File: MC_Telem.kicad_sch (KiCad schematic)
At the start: 59 parts, among them J1 Conn_ARM_JTAG_SWD_10, J2 USB_B_Micro, J3 34830-0801, J5 Conn_01x05, J7 DB37_Male_MountingHoles, J8 34830-0801, J9 GPS, Q1 Q_NMOS_GDS, Q2 Q_NMOS_GDS, Q20 AO4407A, U1 STM32F072RBTx, U2 TPS2113, U3 TCAN1042xV, U4 AMS1117-5.0, U5 AMS1117, U6 LSM6DS3, U7 LTC2630, U8 LTC2630, U9 RFD900x

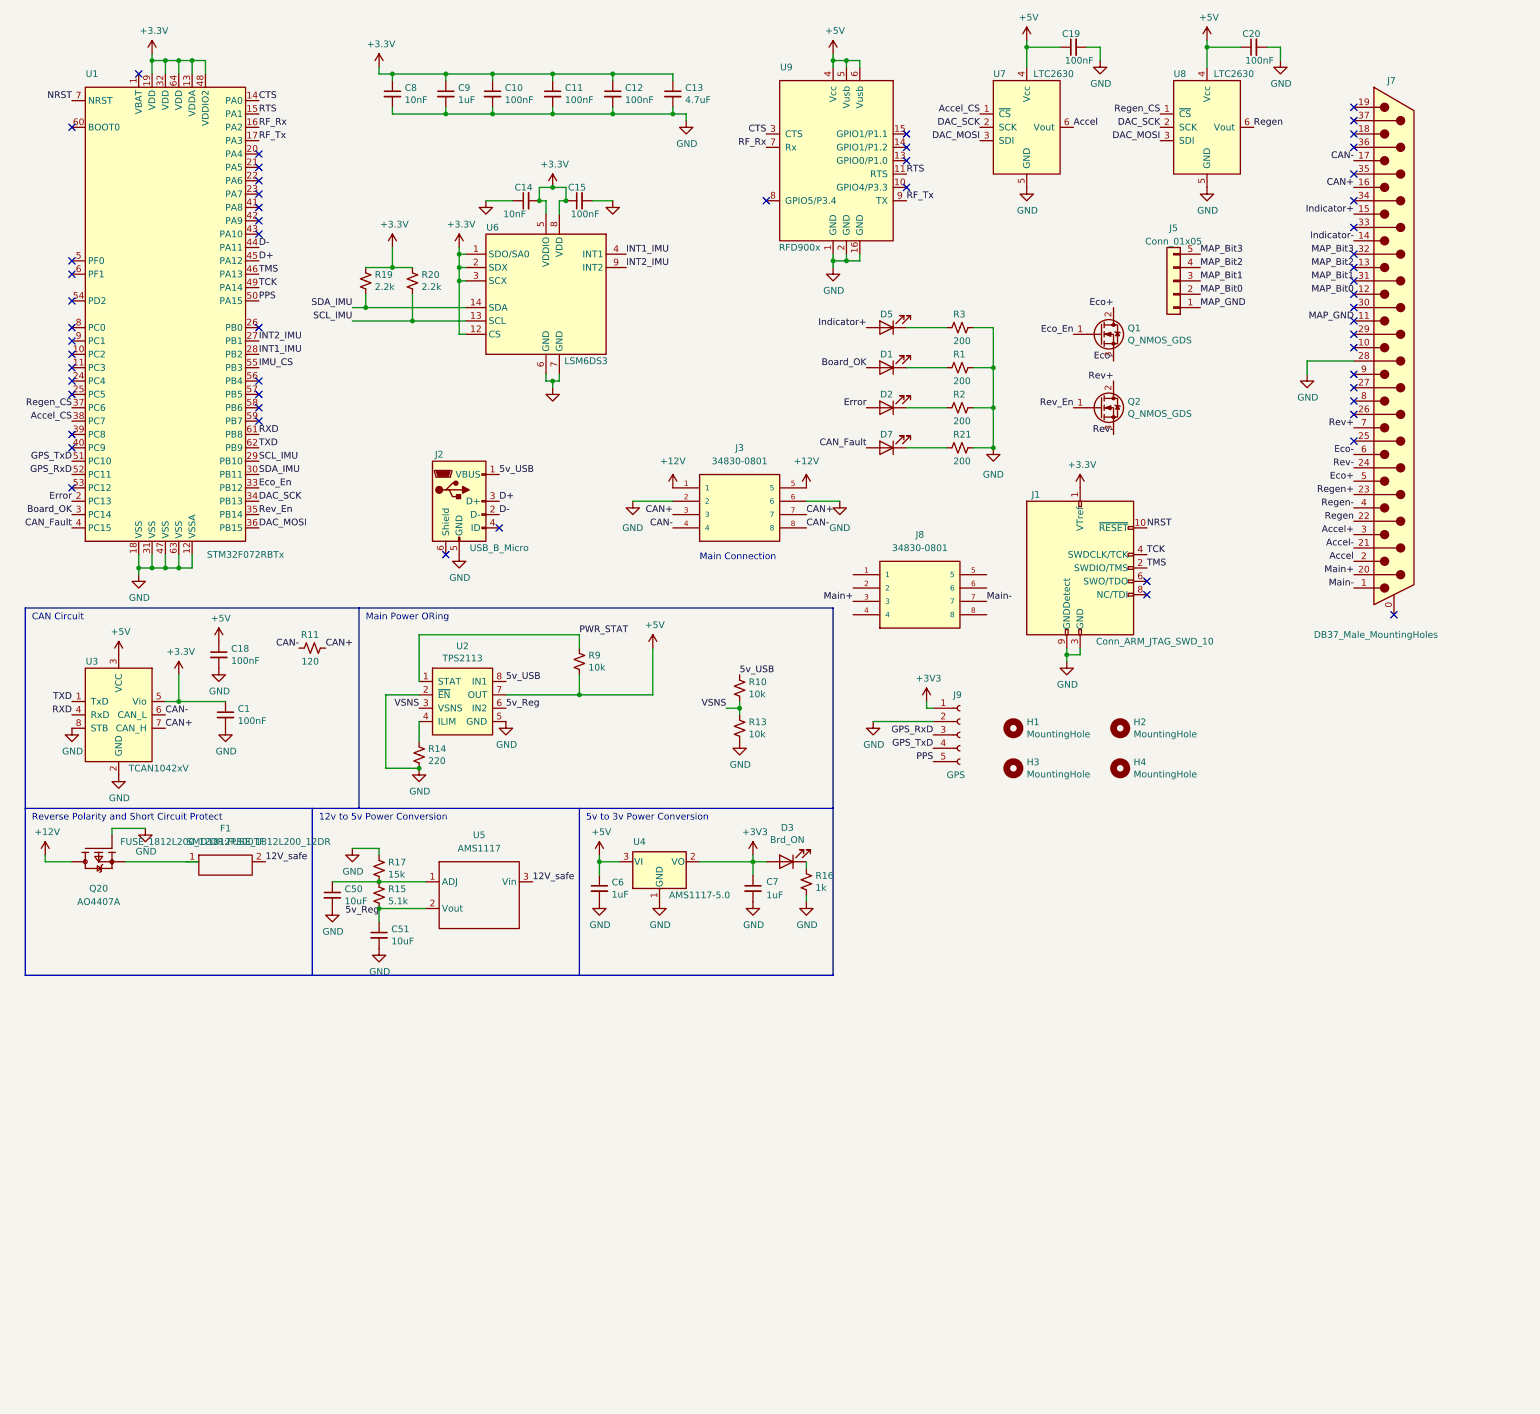
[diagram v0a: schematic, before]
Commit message: FSGP MC Telemetry Hardware
Final PCB revision used for Sunrider at FSGP 2023
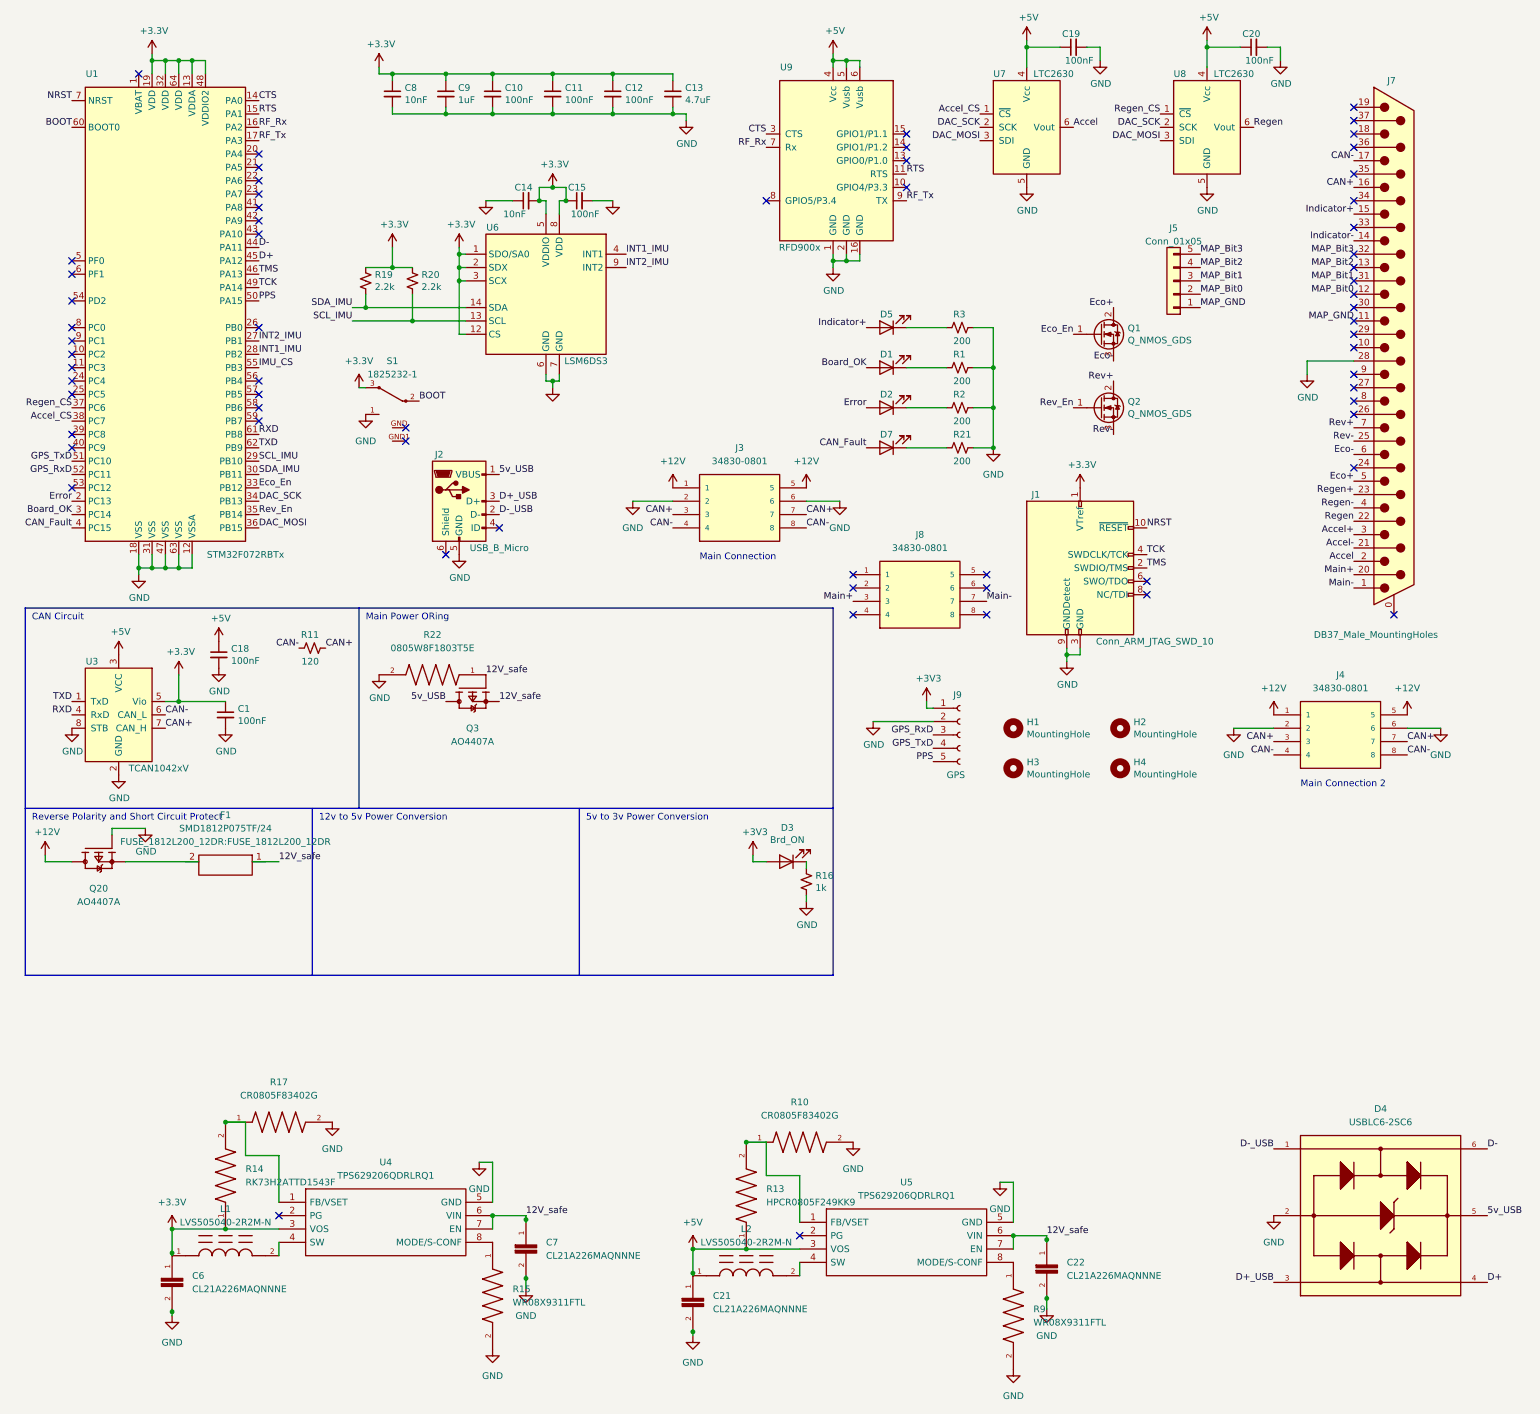
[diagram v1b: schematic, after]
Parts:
- removed C50, C51: 10uF, Capacitor_SMD:C_0402_1005Metric, symbol Device:C_Small
- removed C6, C7: 1uF, Capacitor_SMD:C_0402_1005Metric, symbol Device:C_Small
- removed R10, R13, R9: 10k, Resistor_SMD:R_0603_1608Metric, symbol Device:R_Small_US
- removed R14: 220, Resistor_SMD:R_0603_1608Metric, symbol Device:R_Small_US
- removed R15: 5.1k, Resistor_SMD:R_0603_1608Metric, symbol Device:R_Small_US
- removed R17: 15k, Resistor_SMD:R_0603_1608Metric, symbol Device:R_Small_US
- removed U2: TPS2113, Package_SO:TSSOP-8_4.4x3mm_P0.65mm, symbol JohnLib:TPS2113
- removed U4: AMS1117-5.0, Package_TO_SOT_SMD:SOT-223-3_TabPin2, symbol Regulator_Linear:AMS1117-5.0
- removed U5: AMS1117, AMS1117 (1):SOT229P700X180-4N, symbol New_Library:AMS1117
- added C21, C22, C6, C7: CL21A226MAQNNNE, CAPC2012X140N, symbol CL21A226MAQNNNE:CL21A226MAQNNNE
- added D4: USBLC6-2SC6, SOT95P280X145-6N, symbol USBLC6-2SC6:USBLC6-2SC6
- added J4: 34830-0801, MOLEX_34830-0801, symbol 34830-0801:34830-0801
- added L1, L2: LVS505040-2R2M-N, IND_SDR0403-2R2ML, symbol SDR0403-2R2ML:SDR0403-2R2ML
- added Q3: AO4407A, SOIC127P600X175-8N, symbol AO4407A:AO4407A
- added R10, R17: CR0805F83402G, RESC2012X60N, symbol CR0805AJ_-000EAS:CR0805AJ/-000EAS
- added R13: HPCR0805F249KK9, RESC2012X60N, symbol CR0805AJ_-000EAS:CR0805AJ/-000EAS
- added R14: RK73H2ATTD1543F, RESC2012X60N, symbol CR0805AJ_-000EAS:CR0805AJ/-000EAS
- added R15, R9: WR08X9311FTL, RESC2012X60N, symbol CR0805AJ_-000EAS:CR0805AJ/-000EAS
- added R22: 0805W8F1803T5E, RESC2012X60N, symbol CR0805AJ_-000EAS:CR0805AJ/-000EAS
- added S1: 1825232-1, 1825232-1, symbol 1825232-1:1825232-1
- added U4, U5: TPS629206QDRLRQ1, SOTFL50P160X60-8N, symbol SamacSys_Parts:TPS629206QDRLRQ1
- F1: value SMD1812P300TF -> SMD1812P075TF/24
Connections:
- net +12V: now also J4.1, J4.5
- net +3V3: now also C6.1, L1.1, R14.1, S1.3, U4.3 (VOS)
- net +5V: now also C21.1, L2.1, R13.1, U5.3 (VOS)
- net 12V_safe: now also F1.1, C22.1, C7.1, Q3.1, Q3.2, Q3.3, Q3.4, R22.1, U4.6 (VIN), U4.7 (EN), U5.6 (VIN), U5.7 (EN)
- net 5v_USB: now also D4.5, Q3.5, Q3.6, Q3.7, Q3.8
- net CAN+: now also J4.3, J4.7
- net CAN-: now also J4.4, J4.8
- net D+: now also D4.4; no longer J2.3 (D+)
- net D-: now also D4.6; no longer J2.2 (D-)
- net GND: now also C21.2, C22.2, C6.2, C7.2, D4.2, J4.2, J4.6, R10.2, R15.2, R17.2, R22.2, R9.2, S1.1, U4.5 (GND), U5.5 (GND)
- net Rev-: now also J7.25; no longer J7.24
- net BOOT: now reaches U1.60 (BOOT0)
- net BOOT: now also S1.2
- net at Q20.1, Q20.2, Q20.3: now also F1.2; no longer F1.1
- new net: R15.1, U4.8 (MODE/S-CONF)
- new net: R10.1, R13.2, U5.1 (FB/VSET)
- new net: R14.2, R17.1, U4.1 (FB/VSET)
- new net: L1.2, U4.4 (SW)
- new net: R9.1, U5.8 (MODE/S-CONF)
- new net: L2.2, U5.4 (SW)
- new net D+_USB: D4.3, J2.3 (D+)
- new net D-_USB: D4.1, J2.2 (D-)
- no-connect marks 56 -> 65
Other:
- note added: "Main Connection 2"
